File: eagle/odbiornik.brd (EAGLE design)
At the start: 55.8 x 29.5 mm, 28 parts, among them IC1 MEGA8-AI, IC2 75176AD, IC4 LD117ADT-TR, T1 BC847, T2 BC847, T3 BC847

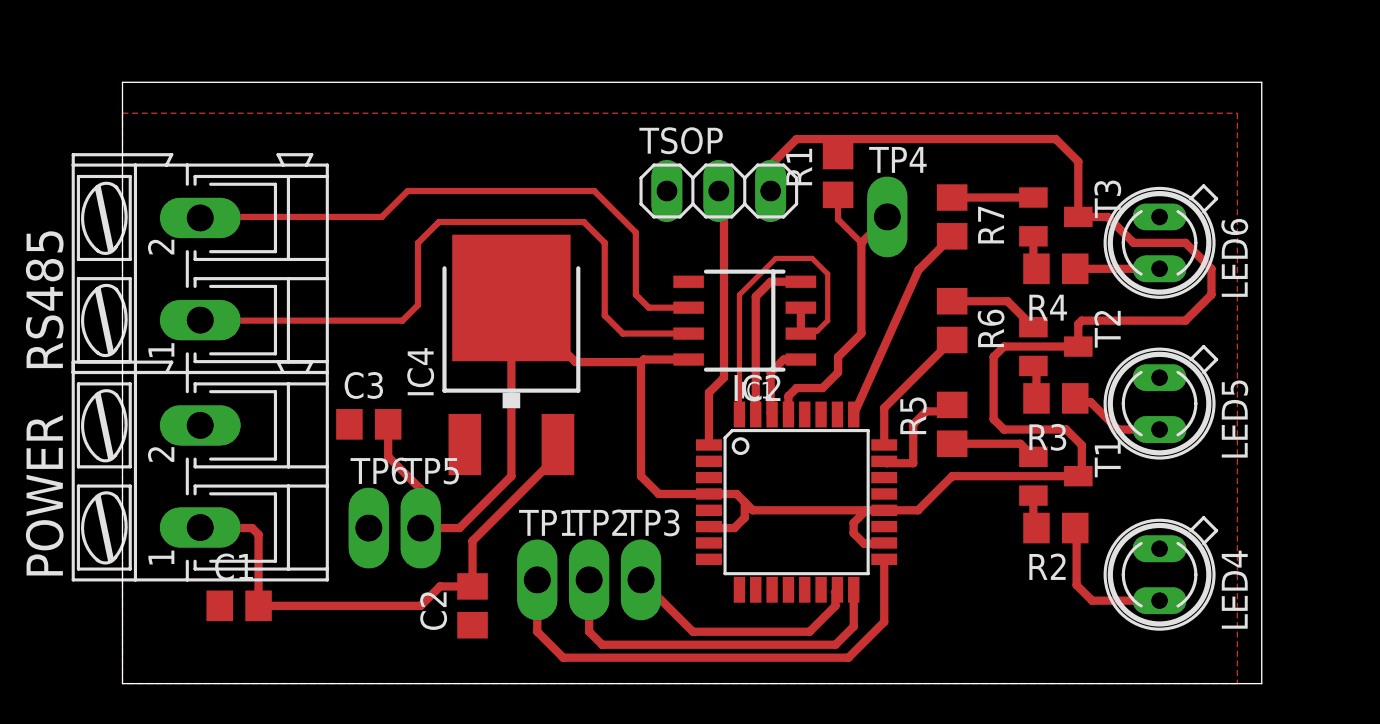
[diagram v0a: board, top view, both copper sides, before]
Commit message: Zmiany: Odbiornik	+Polaryzacja 			+Terminator 			+Poprawki TSOP 			+ISP Socket 			+Power LED Dodano: RS485<->USB - v. poprawiona
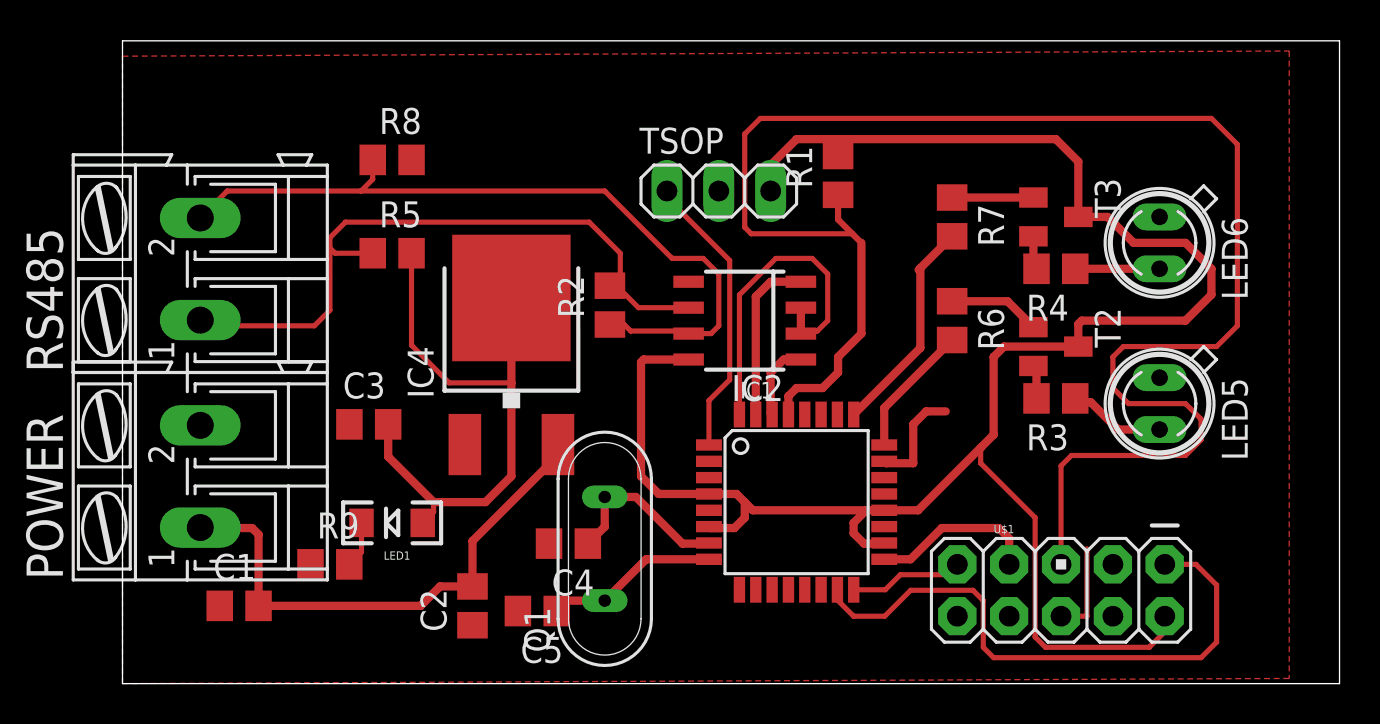
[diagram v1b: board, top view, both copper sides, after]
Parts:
- removed LED4: (no value), led:SFH480
- removed T1: BC847, transistor:SOT23
- removed TP1, TP2, TP3, TP4, TP5, TP6: TPPAD1-13Y, testpad:P1-13Y
- added C4, C5: 18p, rcl:C0805
- added LED1: (no value), SparkFun-LED:LED-1206
- added Q1: 16MHz, special:QS
- added R8: 750, rcl:R0805
- added R9: 500, rcl:R0805
- added U$1: AVR_SPI_PROG2PTH, SparkFun-Connectors:AVR_ICSP
- R2: value (none) -> 130
- R5: value (none) -> 750
- moved R5 28.7 mm to (13.2, 21.1), turned to 0 degrees
- moved R2 24.4 mm to (23.9, 18.5), turned to 90 degrees
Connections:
- removed net N$2: LED4.A, R2.1
- removed net N$7: R5.1, T1.1
- new net N$10: C5.1, IC1.8, Q1.1
- new net N$11: C4.1, IC1.7, Q1.2
- net GND: now also C4.2, C5.2, R8.2, R9.1, TSOP.2, U$1.10, U$1.4, U$1.6, U$1.8; no longer LED4.K, TP6.TP, TSOP.1
- net LED1: no longer R5.2
- net MISO: now also U$1.9; no longer TP2.TP
- net MOSI: now also U$1.1; no longer TP3.TP
- net N$1: now also LED1.C, R9.2; no longer R2.2, T1.2
- net RSA: now also R2.2, R5.1, RS485.1; no longer RS485.2
- net RSB: now also R2.1, R8.1, RS485.2; no longer RS485.1
- net RST: now also U$1.5; no longer TP4.TP
- net SCK: now also U$1.7; no longer TP1.TP
- net TSOP: now also TSOP.1; no longer TSOP.2
- net VCC: now also LED1.A, R5.2, U$1.2; no longer T1.3, TP5.TP
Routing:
- net RST: track 15.3 -> 83.7 mm
- net MOSI: track 11.9 -> 28.7 mm
- net SCK: track 23.9 -> 8.24 mm
- net MISO: track 17.9 -> 5.59 mm
- net VCC: track 116.0 -> 126.6 mm
- net N$11: track 0.00 -> 8.69 mm
- net N$10: track 0.00 -> 8.51 mm
- net N$2: track 7.20 -> 0.00 mm
- net RSB: track 32.1 -> 38.4 mm
- net RSA: track 28.6 -> 33.7 mm
- net GND: track 0.00 -> 4.57 mm
- net N$7: track 4.25 -> 0.00 mm
- net TSOP: track 12.9 -> 14.1 mm
- net LED3: track 10.1 -> 10.8 mm
- net N$1: track 1.65 -> 2.28 mm
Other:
- board size 55.8 x 29.5 mm -> 59.6 x 31.5 mm

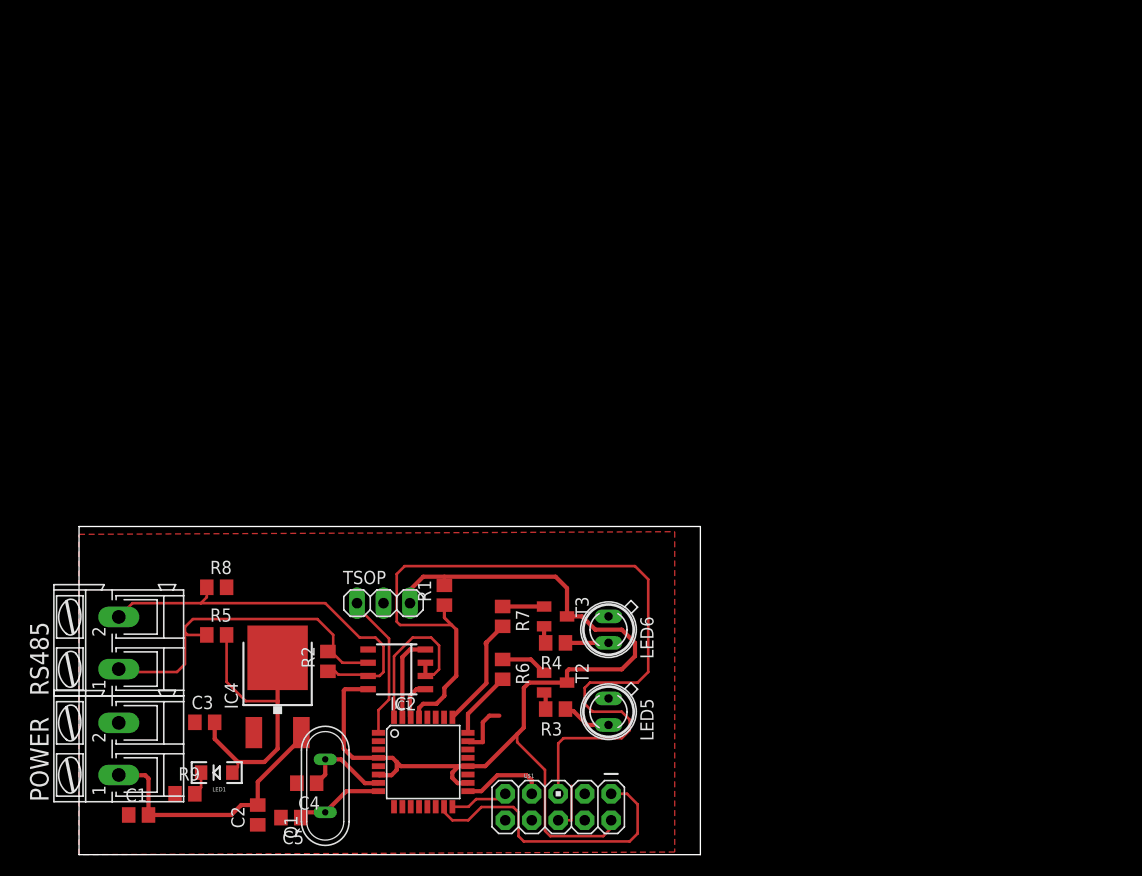
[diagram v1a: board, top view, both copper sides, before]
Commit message: New Receiver Board + Schematic + Gitignore prototype
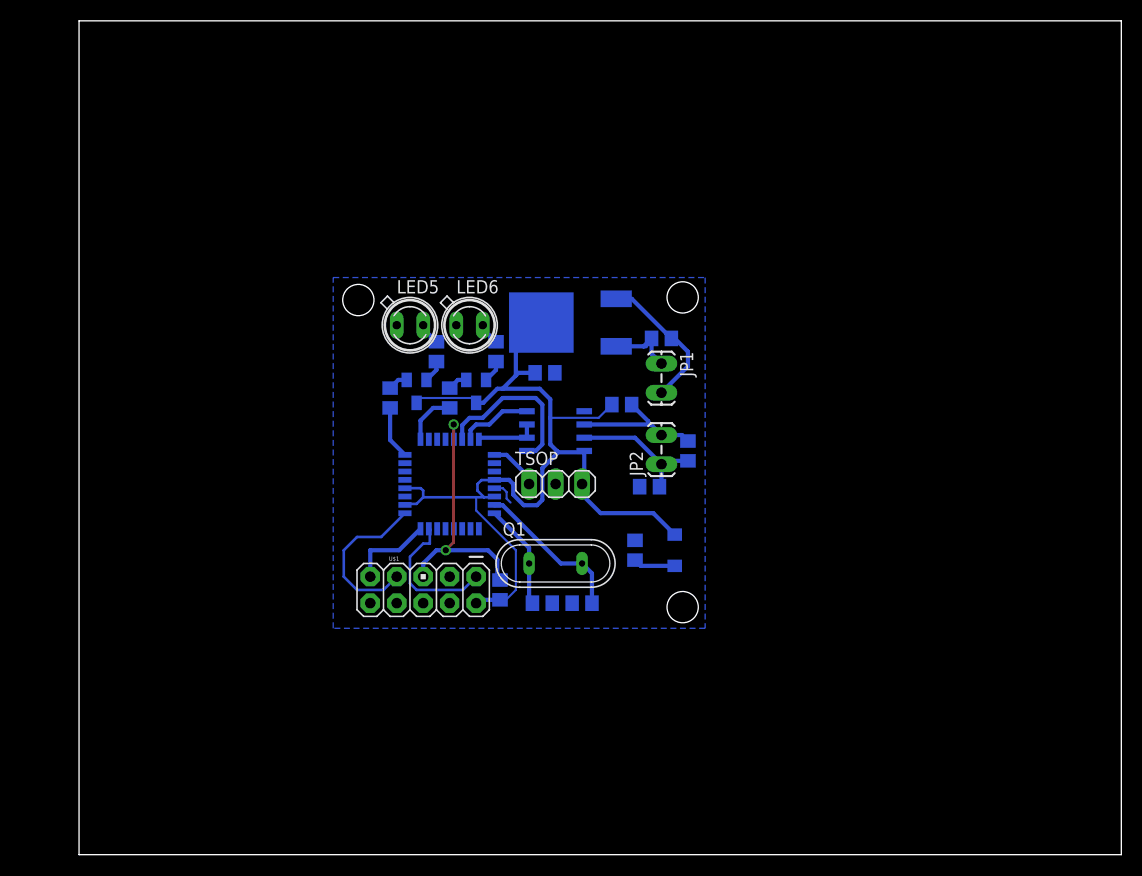
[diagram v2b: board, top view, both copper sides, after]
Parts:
- removed C1: (no value), rcl:C0805
- removed POWER, RS485: (no value), con-ptr500:AK300/2
- added JP1, JP2: (no value), SparkFun-Connectors:1X02_LOCK_LONGPADS
- moved C2 59.9 mm to (55.9, 49.5), flipped to the bottom, turned to 0 degrees
- moved R9 49.1 mm to (53.3, 29.2), flipped to the bottom, turned to 270 degrees
- moved LED1 48.8 mm to (57.1, 29.2), flipped to the bottom, turned to 270 degrees
- moved C3 46.8 mm to (44.7, 46.2), flipped to the bottom
- moved R5 44.7 mm to (52.1, 43.2), flipped to the bottom
- moved IC4 44.3 mm to (46.7, 51.1), flipped to the bottom, turned to 270 degrees
- moved R8 42.6 mm to (54.7, 35.3), flipped to the bottom
- moved LED5 41.7 mm to (31.8, 50.8), turned to 0 degrees
- moved R2 40.0 mm to (58.4, 38.7), flipped to the bottom
- moved R3 36.1 mm to (34.3, 48.3), flipped to the bottom, turned to 270 degrees
- moved LED6 32.1 mm to (37.5, 50.8), turned to 0 degrees
- moved C5 31.7 mm to (44.5, 24.1), flipped to the bottom
- moved C4 31.6 mm to (48.3, 24.1), flipped to the bottom, turned to 0 degrees
- moved T2 31.0 mm to (32.4, 44.5), flipped to the bottom, turned to 180 degrees
- moved Q1 30.7 mm to (45.7, 27.9), turned to 0 degrees
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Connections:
- net 12V: now also JP1.1; no longer C1.2, POWER.1
- net GND: now also JP1.2; no longer C1.1, POWER.2
- net RSA: now also JP2.2; no longer RS485.1
- net RSB: now also JP2.1; no longer RS485.2
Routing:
- net RST: track 83.7 -> 25.2 mm, vias 0 -> 2
- net VCC: track 126.6 -> 94.8 mm
- net RSB: track 38.4 -> 13.8 mm
- net RSA: track 33.7 -> 13.2 mm
- net 12V: track 26.0 -> 6.81 mm
- net MOSI: track 28.7 -> 13.6 mm
- net GND: track 4.57 -> 17.7 mm
- net RXD: track 3.83 -> 15.9 mm
- net DATA: track 16.4 -> 5.94 mm
- net TSOP: track 14.1 -> 4.86 mm
- net SCK: track 8.24 -> 16.0 mm
- net N$11: track 8.69 -> 14.9 mm
- net LED3: track 10.8 -> 5.10 mm
- net LED1: track 5.22 -> 0.00 mm
- net N$3: track 4.87 -> 2.12 mm
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- added copper zone on layer 16, net GND
- removed copper zone on layer 1, net GND
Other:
- board size 59.6 x 31.5 mm -> 100 x 80 mm
